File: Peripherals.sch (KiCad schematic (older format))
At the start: 62 parts, among them J10 Conn_01x01, J11 Conn_01x01, J12 Conn_01x01, J13 Conn_01x04, J14 RCAJack, J5 Conn_01x10, J6 Conn_01x10, J7 Conn_01x10, J8 Conn_01x08, J9 Conn_01x01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

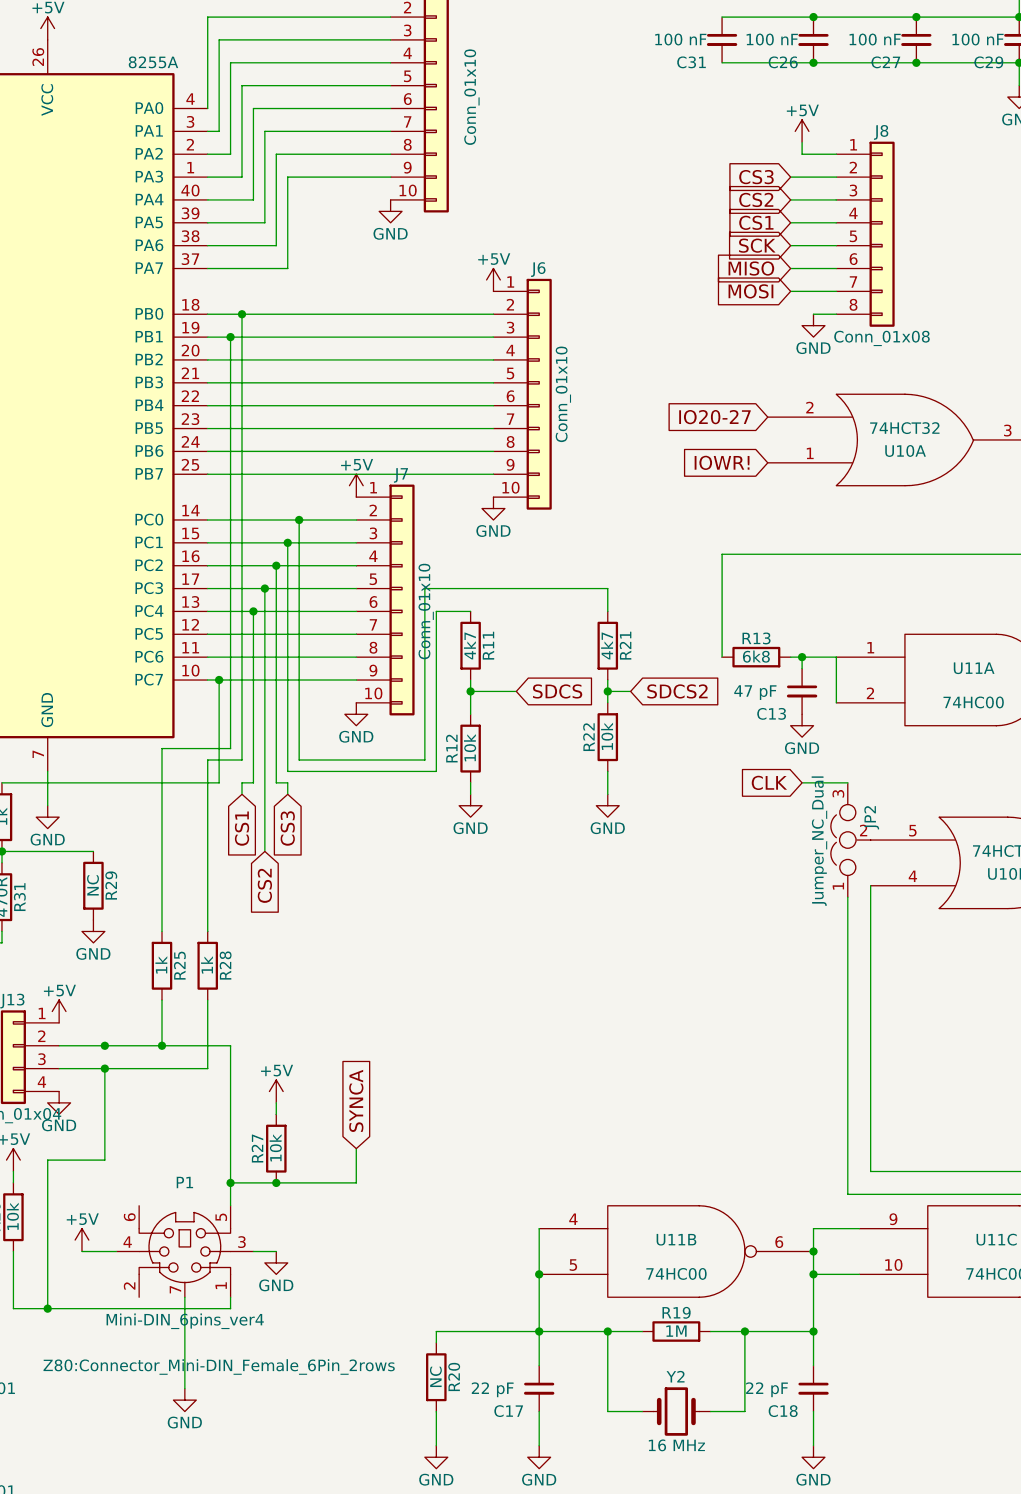
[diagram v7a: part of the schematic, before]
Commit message: Moved around port B/C pins to separate input and output groups
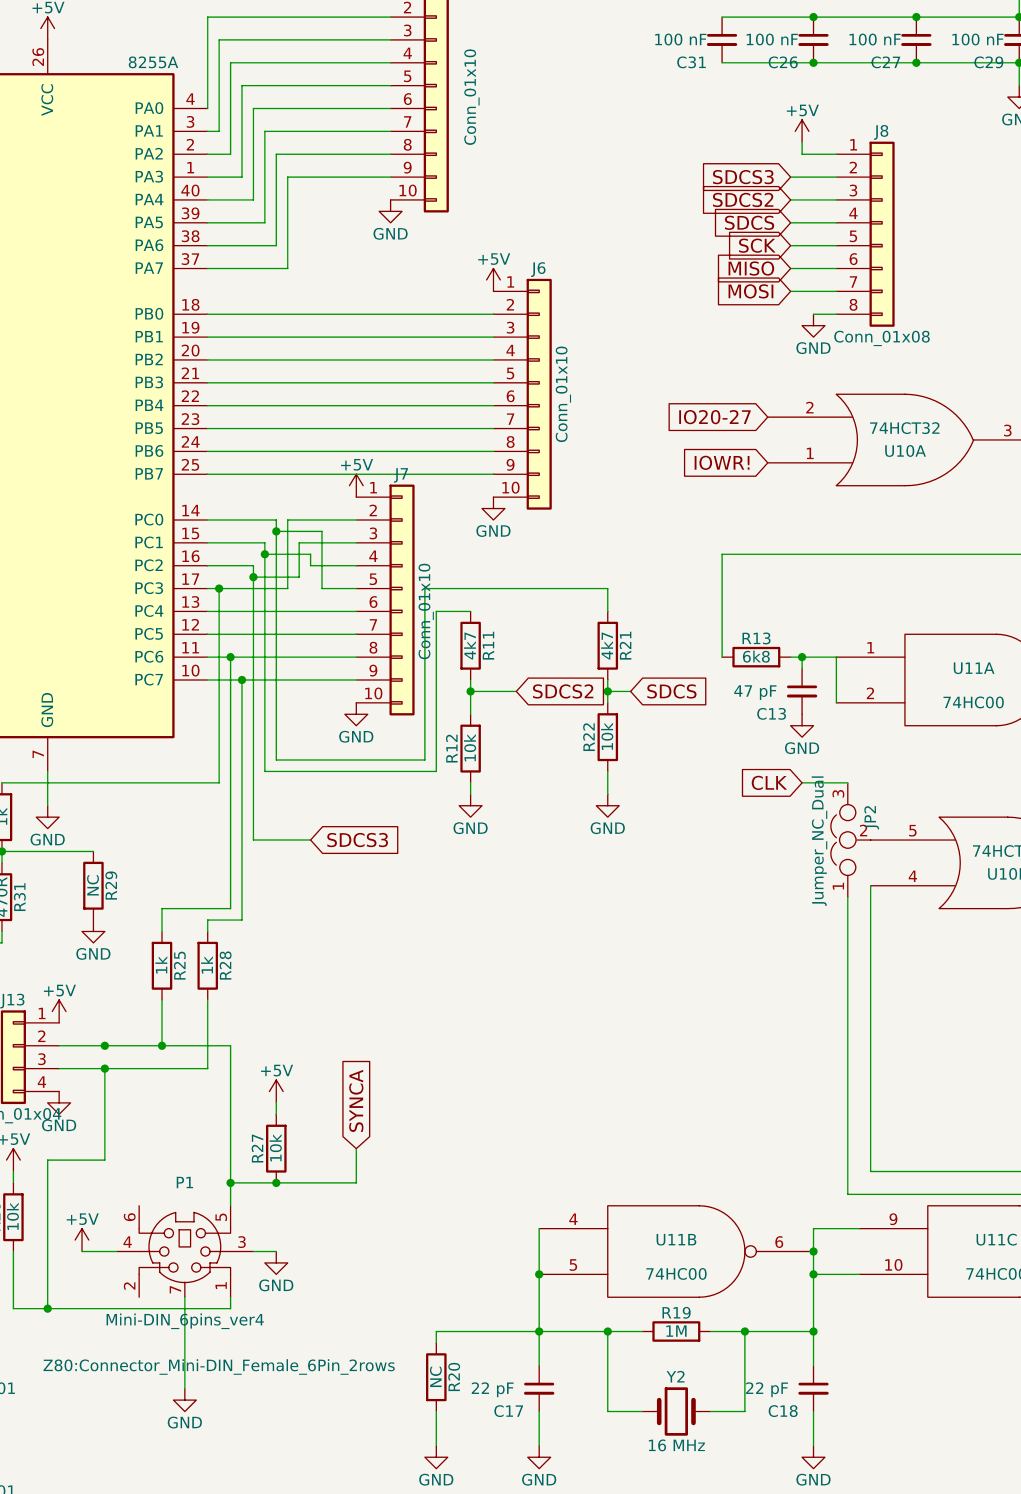
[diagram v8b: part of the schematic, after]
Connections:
- net SDCS: now also J8.4 (Pin_4), R21.2, R22.2; no longer R11.2, R12.2
- net SDCS2: now also J8.3 (Pin_3), R11.2, R12.2; no longer R21.2, R22.2
- net at R11.1, U9.15 (PC1): now also J7.4 (Pin_4); no longer J7.3 (Pin_3)
- net at R21.1, U9.14 (PC0): now also J7.5 (Pin_5); no longer J7.2 (Pin_2)
- net at J6.2 (Pin_2), U9.18 (PB0): no longer R28.2
- net at J6.3 (Pin_3), U9.19 (PB1): no longer R25.2
- net at J7.8 (Pin_8), U9.11 (PC6): now also R25.2
- net at J7.9 (Pin_9), U9.10 (PC7): now also R28.2; no longer R30.2
- net CS1: no longer names the net of J7.6 (Pin_6), U9.13 (PC4)
- net CS1: no longer J8.4 (Pin_4)
- removed net CS2: J7.5 (Pin_5), J8.3 (Pin_3), U9.17 (PC3)
- net CS3 renamed SDCS3
- net SDCS3: now also J7.3 (Pin_3); no longer J7.4 (Pin_4)
- new net: J7.2 (Pin_2), R30.2, U9.17 (PC3)
